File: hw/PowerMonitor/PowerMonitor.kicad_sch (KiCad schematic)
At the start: 53 parts, among them J1 Conn_01x02_Socket, J2 Conn_01x02_Socket, J3 Conn_01x02_Socket, J4 Conn_01x02_Socket, J5 Conn_01x02_Socket, K1 Relay_SPST-NO, Q1 AO3400A, Q13 X0202MN, Q2 AO3400A, Q20 AO3400A, Q3 AO3400A, SW1 SW_Wuerth_450301014042, U1 LM393, U2 INA129

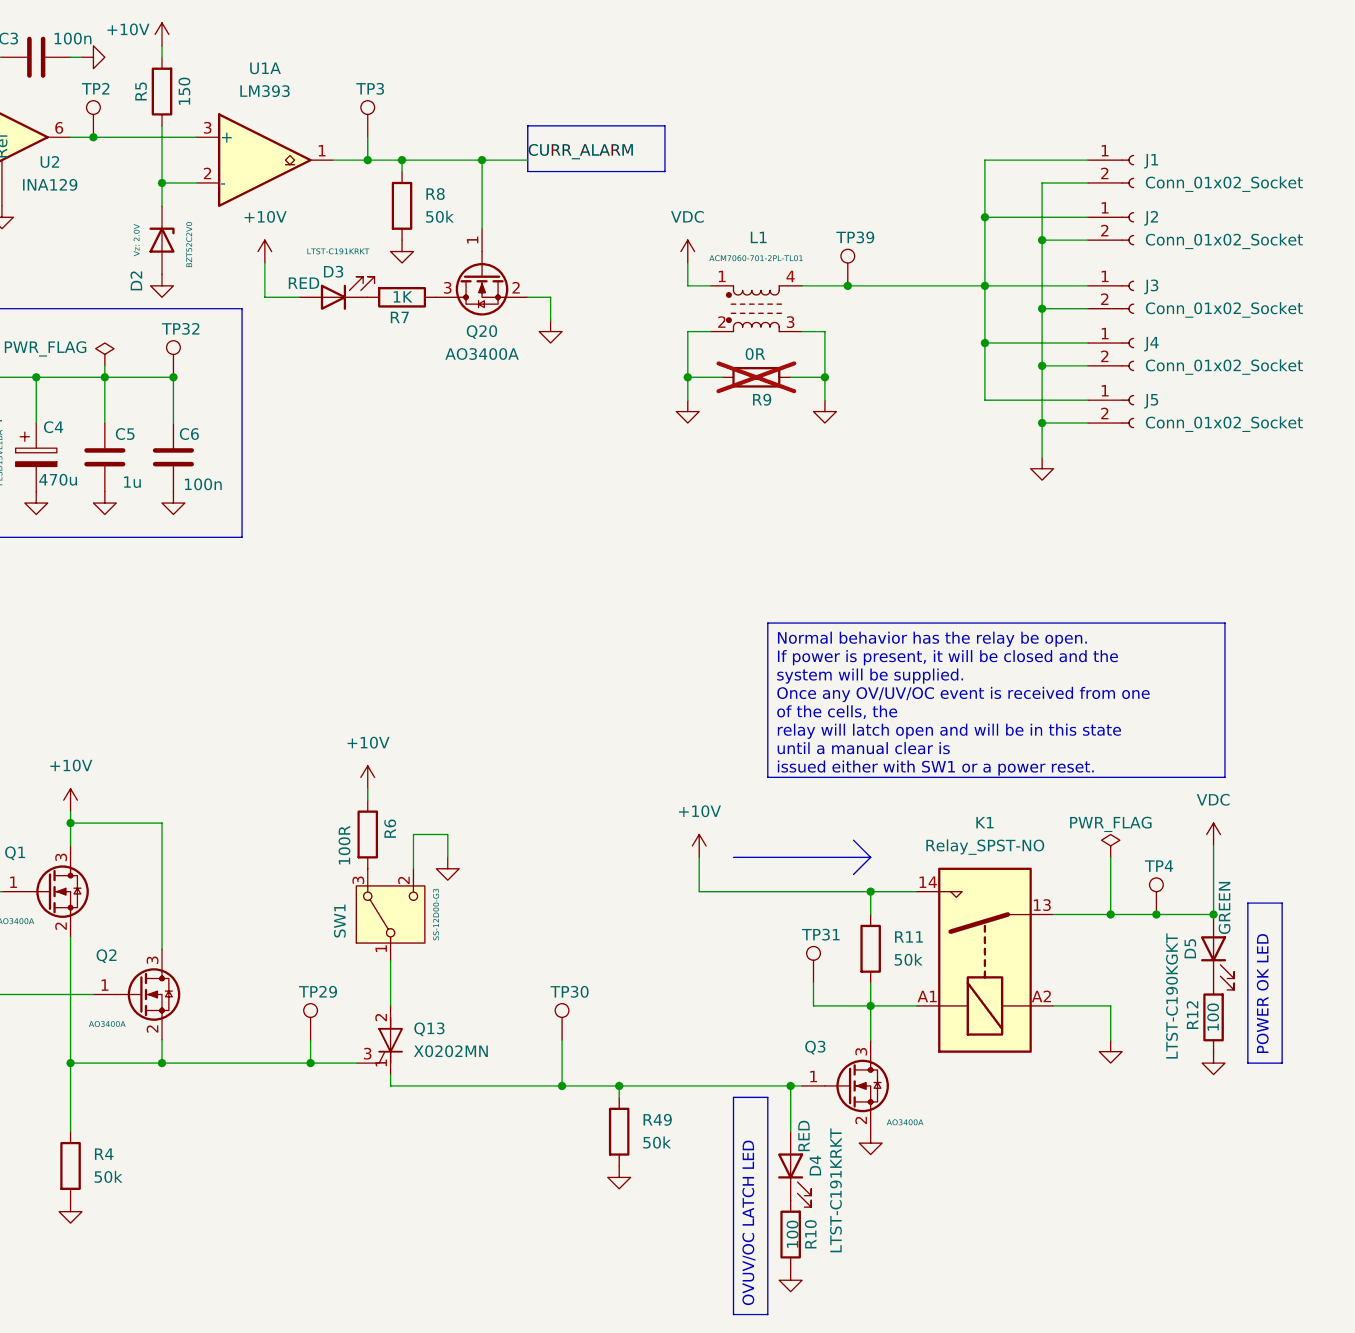
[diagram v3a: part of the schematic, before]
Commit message: finish PowerMonitor placement
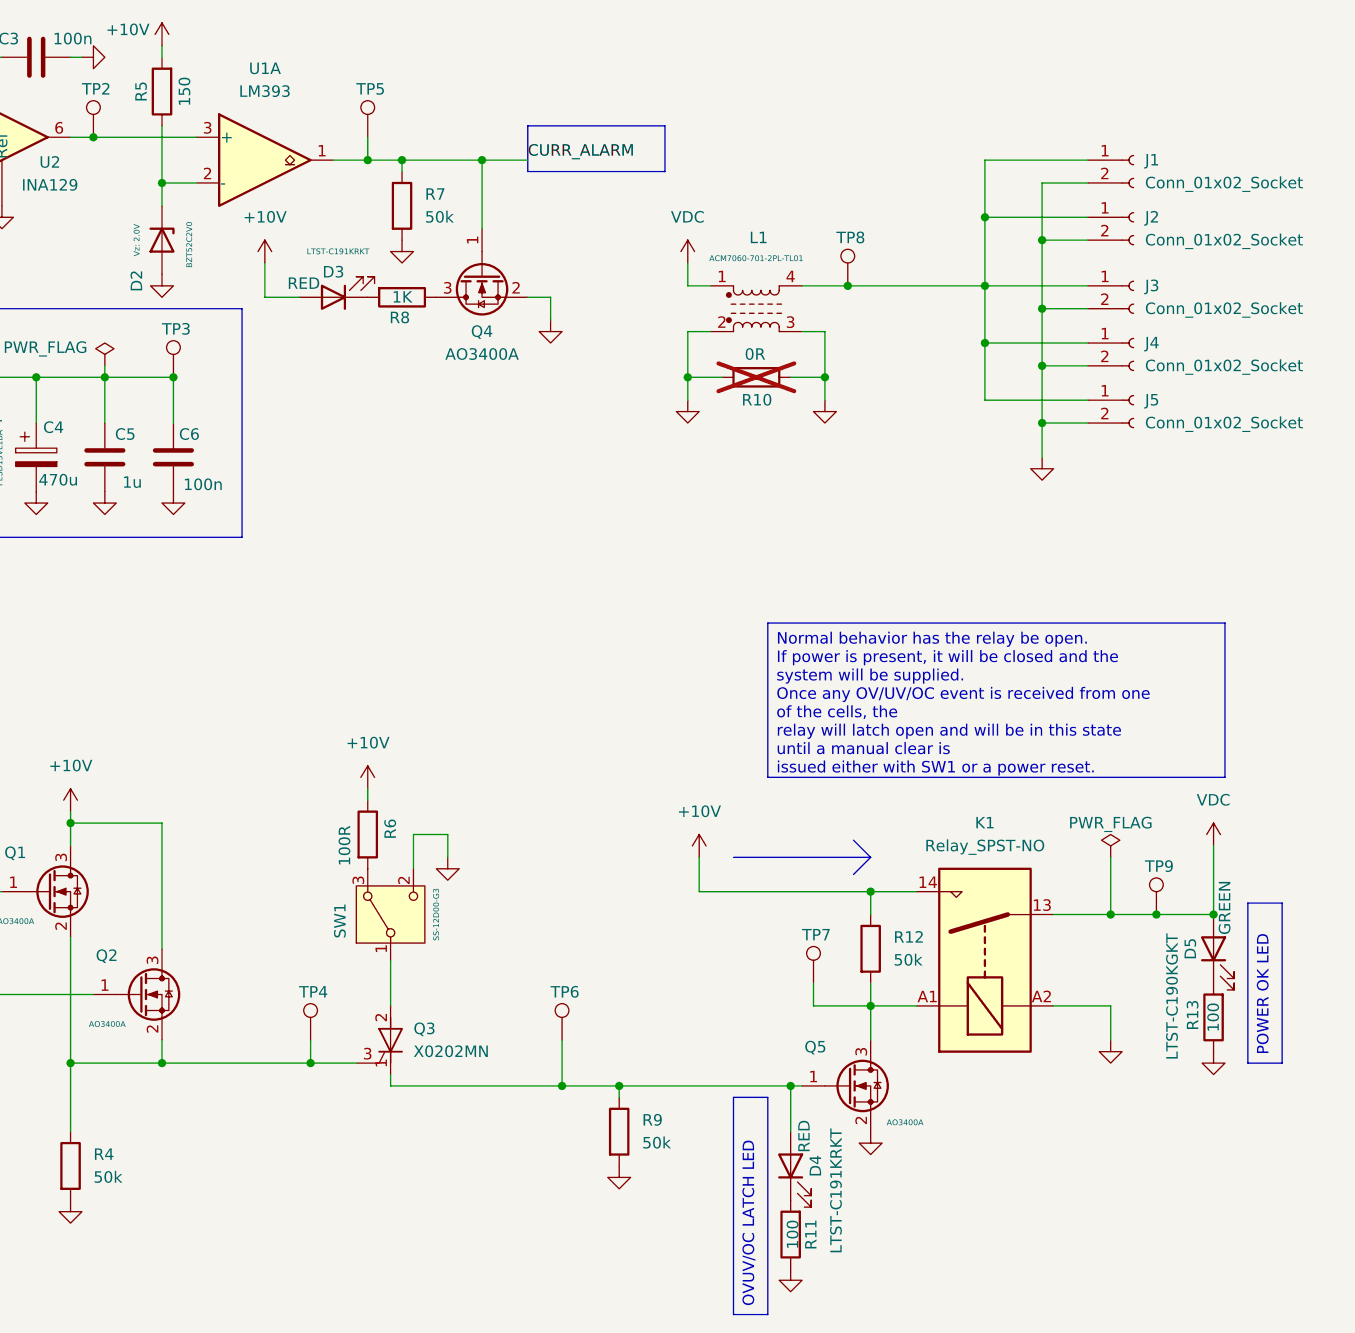
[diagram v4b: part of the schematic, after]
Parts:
- R11: renamed from R10; footprint Resistor_SMD:R_0603_1608Metric -> Resistor_SMD:R_0603_1608Metric_Pad0.98x0.95mm_HandSolder
- R13: renamed from R12; footprint Resistor_SMD:R_0603_1608Metric -> Resistor_SMD:R_0603_1608Metric_Pad0.98x0.95mm_HandSolder
- R8: renamed from R7; footprint Resistor_SMD:R_0603_1608Metric -> Resistor_SMD:R_0603_1608Metric_Pad0.98x0.95mm_HandSolder
- renumbered Q13 to Q3, Q20 to Q4, Q3 to Q5, R9 to R10, R11 to R12, R8 to R7, R49 to R9, TP32 to TP3, TP29 to TP4, TP3 to TP5, TP30 to TP6, TP31 to TP7, TP39 to TP8, TP4 to TP9

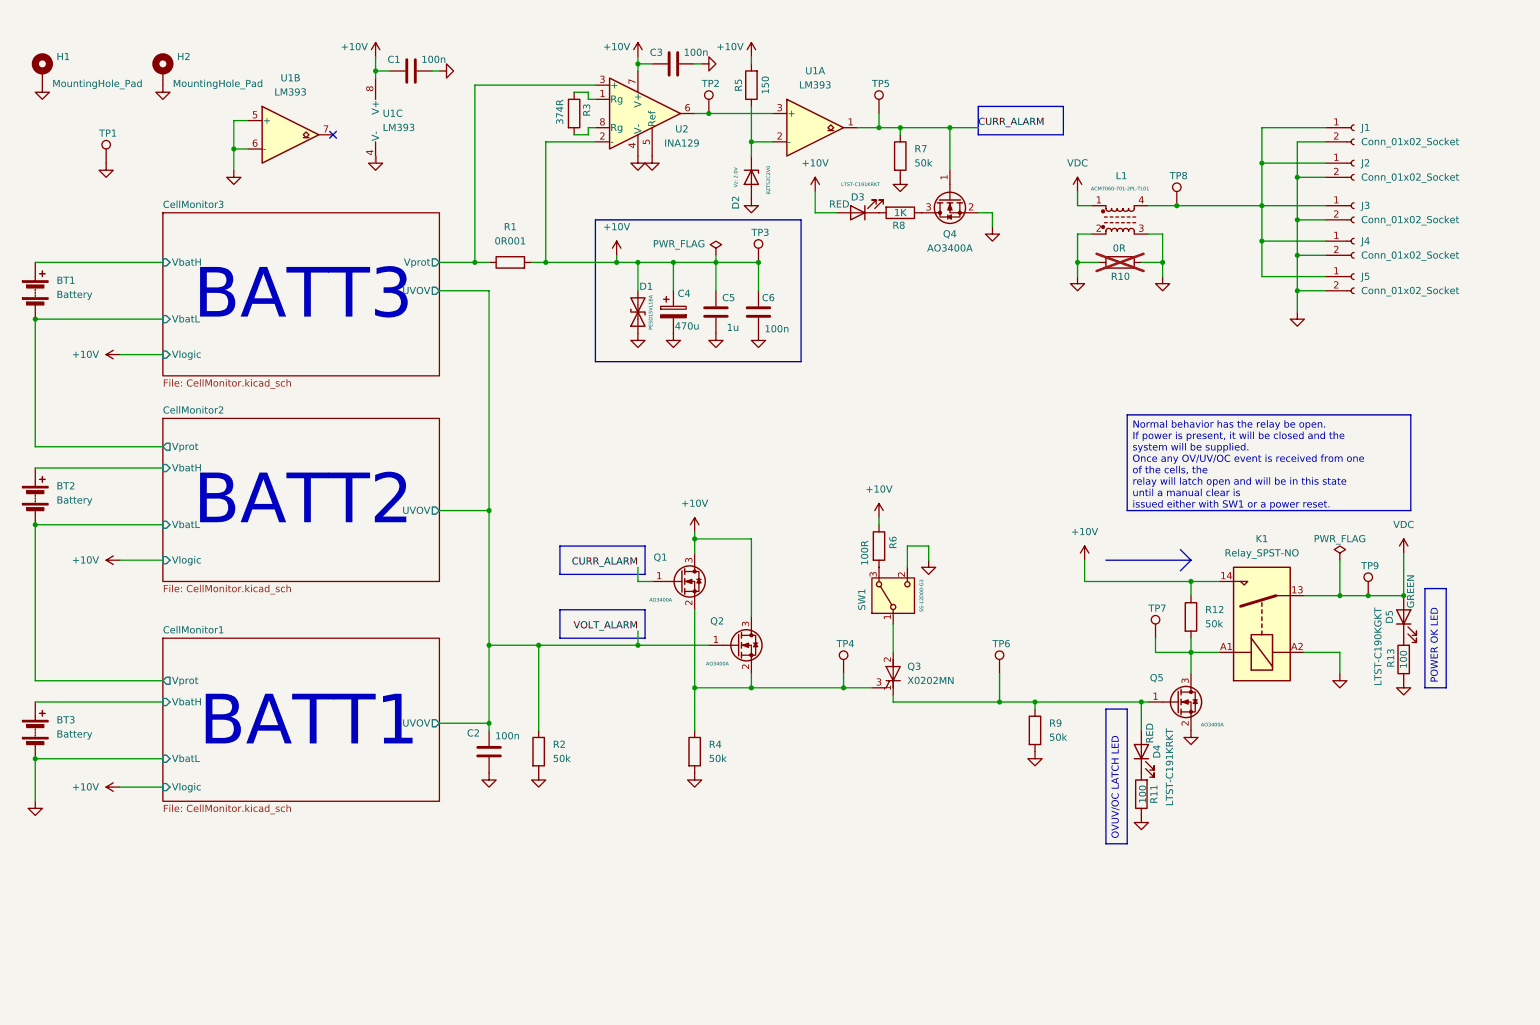
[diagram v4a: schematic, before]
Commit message: powmon: advance routing
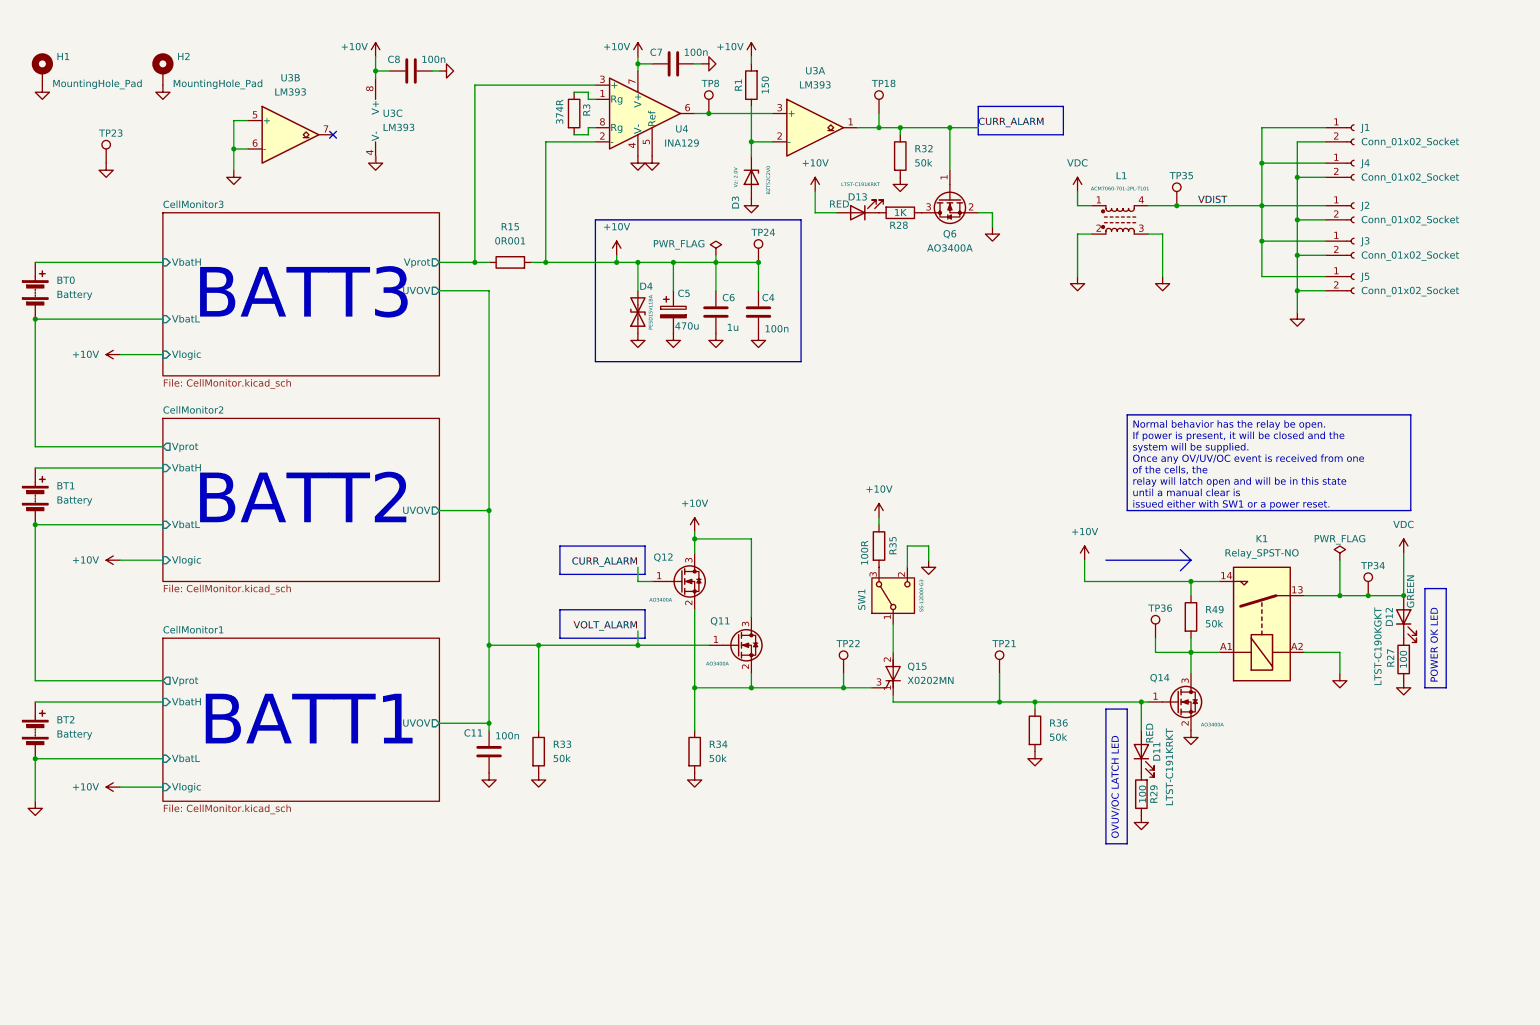
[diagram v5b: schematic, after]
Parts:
- removed R10: 0R, Resistor_SMD:R_0603_1608Metric_Pad0.98x0.95mm_HandSolder, symbol Device:R
- renumbered BT1 to BT0, BT2 to BT1, BT3 to BT2, C2 to C11, C6 to C4, C4 to C5, C5 to C6, C3 to C7, C1 to C8, D4 to D11, D5 to D12, D3 to D13, D2 to D3, D1 to D4, J3 to J2, J4 to J3, J2 to J4, Q2 to Q11, Q1 to Q12, Q5 to Q14, Q3 to Q15, Q4 to Q6, R5 to R1, R1 to R15, R13 to R27, R8 to R28, R11 to R29, R7 to R32, R2 to R33, R4 to R34, R6 to R35, R9 to R36, R12 to R49, TP5 to TP18, TP6 to TP21, TP4 to TP22, TP1 to TP23, TP3 to TP24, TP9 to TP34, TP8 to TP35, TP7 to TP36, TP2 to TP8, U1 to U3, U2 to U4
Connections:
- net VDIST: now reaches J1.1 (Pin_1), J2.1 (Pin_1), J3.1 (Pin_1), J4.1 (Pin_1), J5.1 (Pin_1), L1.4, TP35.1
